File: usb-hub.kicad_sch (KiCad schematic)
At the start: 24 parts, among them U4 USB2422-I_MJ, Y1 Oscillator_24MHz_ESC_2016MV

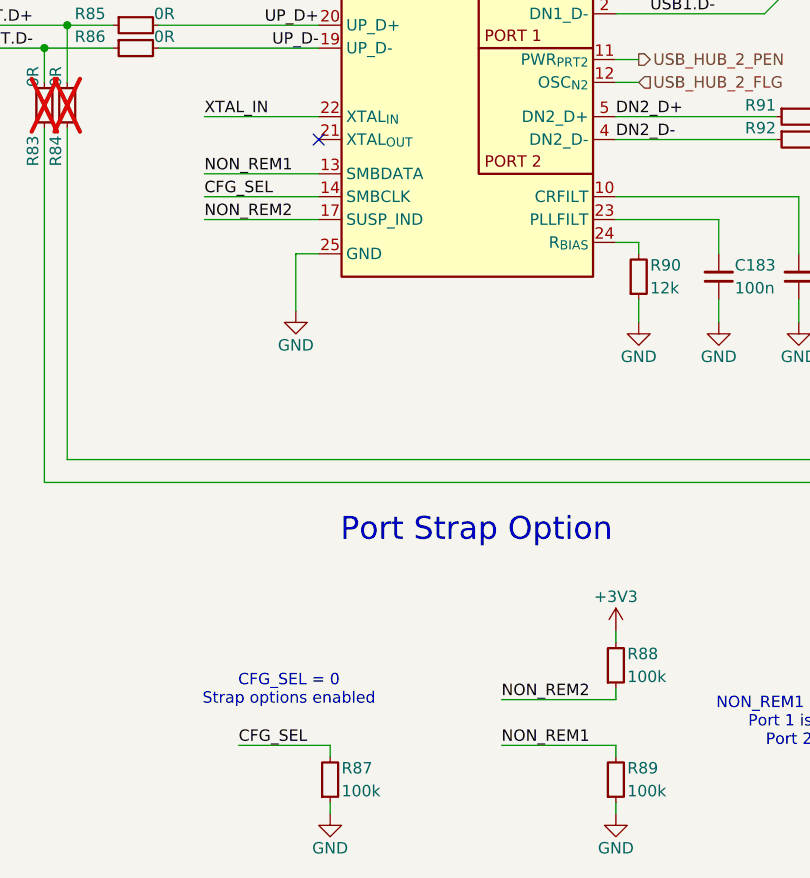
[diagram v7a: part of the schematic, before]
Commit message: [#83767] Cleanup USB2422 REM strap net names
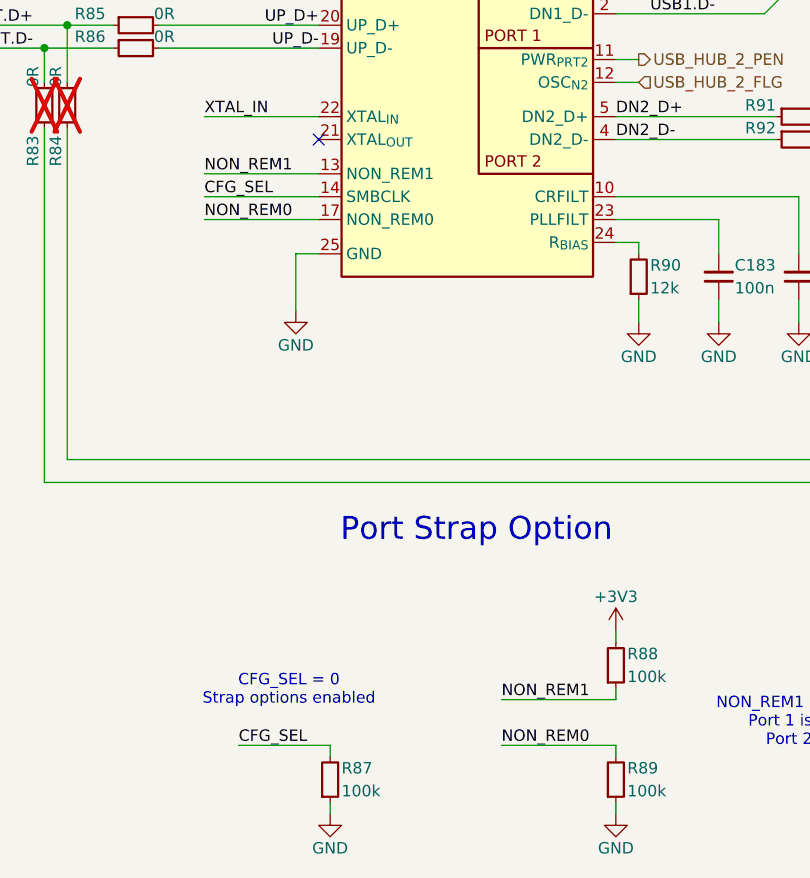
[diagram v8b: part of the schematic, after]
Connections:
- net NON_REM1: now also R88.1; no longer R89.2
- net NON_REM2 renamed NON_REM0
- net NON_REM0: now also R89.2; no longer R88.1
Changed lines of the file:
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@@
 	)
 	(label "NON_REM1"
-		(at 186.69 190.5 0)
+		(at 186.69 185.42 0)
 		(effects
 			(font
@@
 		)
 	)
-	(label "NON_REM2"
+	(label "NON_REM0"
 		(at 153.67 132.08 0)
 		(effects
@@
 		)
 	)
-	(label "NON_REM2"
-		(at 186.69 185.42 0)
+	(label "NON_REM0"
+		(at 186.69 190.5 0)
 		(effects
 			(font
@@
 		)
 		(pin "13"
+			(alternate "NON_REM1")
 		)
 		(pin "18"
@@
 		)
 		(pin "17"
+			(alternate "NON_REM0")
 		)
 		(pin "2"
